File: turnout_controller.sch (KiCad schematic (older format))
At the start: 29 parts, among them J1 DCC_A, J2 DCC_B, J3 PROG, J4 MOT_CNTL, J5 MOT_POWER, J6 MOT_GND, J7 LED_1, J8 LED_2, SW1 SW_Push, SW2 SW_Push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

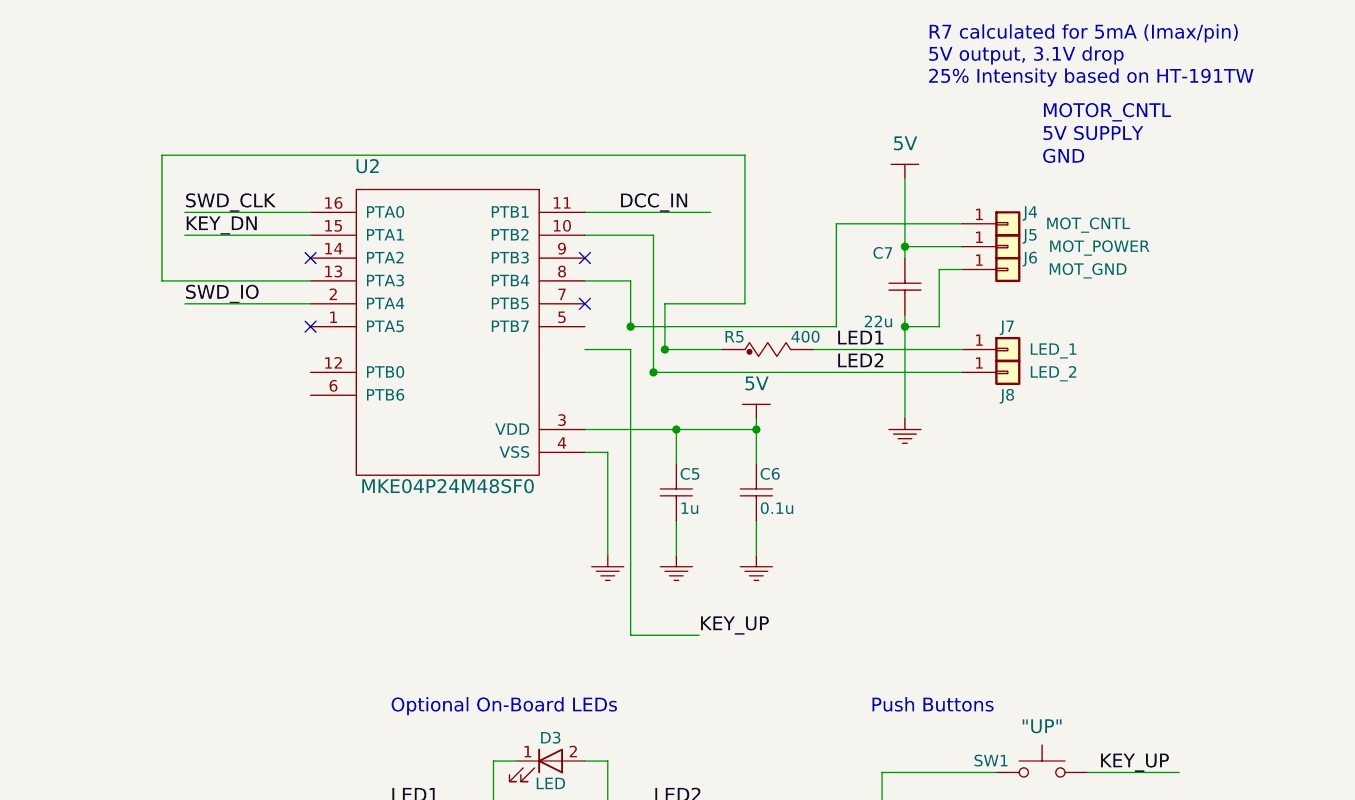
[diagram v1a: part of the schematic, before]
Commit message: Updated schematic for clarity. New Netlist. No PCB changes.
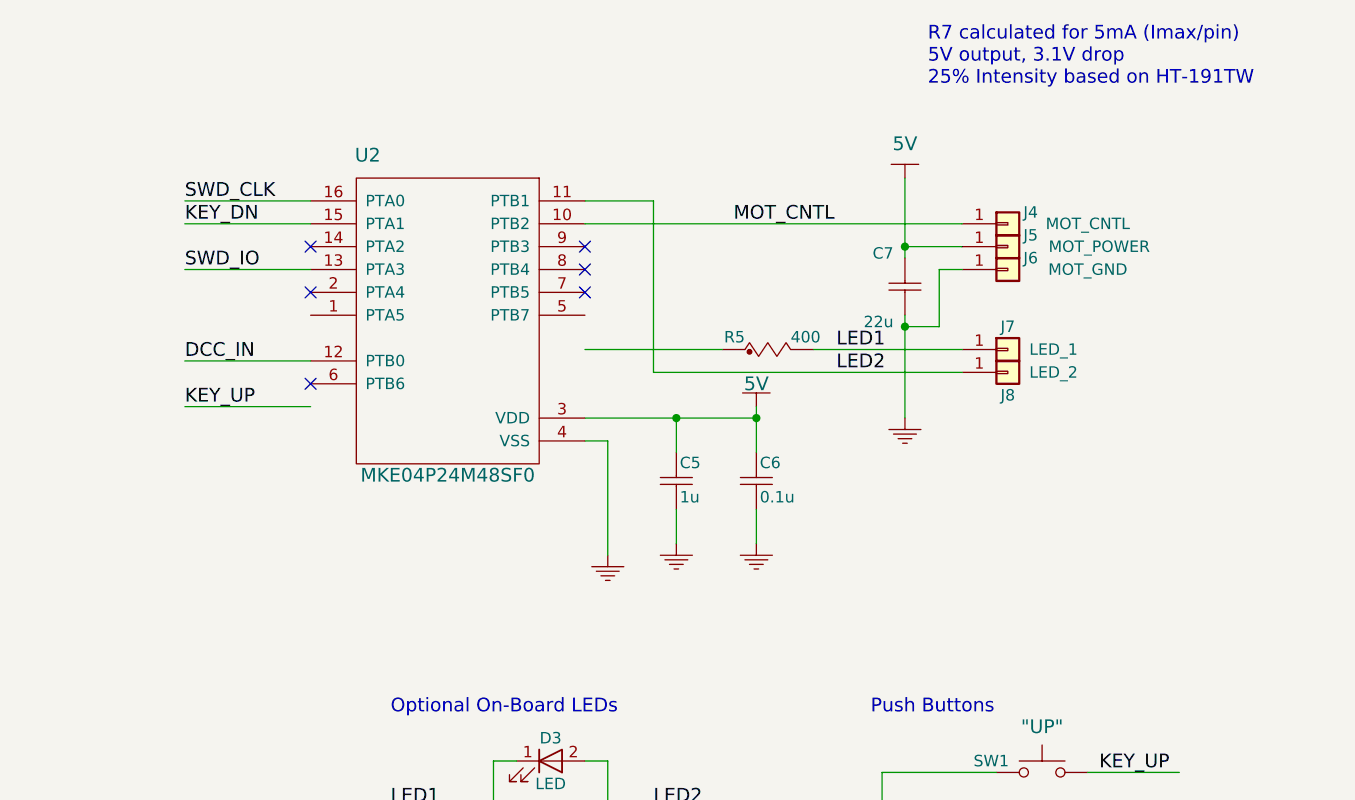
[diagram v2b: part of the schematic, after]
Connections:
- net labels added: MOT_CNTL
- wire segments 94 -> 82
- no-connect marks 4 -> 6
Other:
- note removed: "5V SUPPLY"
- note removed: "GND"
- note removed: "MOTOR_CNTL"
- moved on the sheet: C5, C6, U2
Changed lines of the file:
@@
 EESchema Schematic File Version 2
-LIBS:turnout_controller-rescue
 LIBS:power
 LIBS:device
@@
 L CAP_NP C5
 U 1 1 59FFDD6D
-P 8350 2750
-F 0 "C5" H 8365 2925 50  0000 L BNN
-F 1 "1u" H 8365 2775 50  0000 L BNN
-F 2 "Capacitors_SMD:C_0603_HandSoldering" H 8425 2650 40  0001 L BNN
-F 3 "" H 8350 2750 60  0000 C CNN
-F 4 "Volt" H 8450 2700 40  0001 L BNN "Voltage"
-	1    8350 2750
+P 8350 2700
+F 0 "C5" H 8365 2875 50  0000 L BNN
+F 1 "1u" H 8365 2725 50  0000 L BNN
+F 2 "Capacitors_SMD:C_0603_HandSoldering" H 8425 2600 40  0001 L BNN
+F 3 "" H 8350 2700 60  0000 C CNN
+F 4 "Volt" H 8450 2650 40  0001 L BNN "Voltage"
+	1    8350 2700
 	1    0    0    -1
 $EndComp
@@
 L CAP_NP C6
 U 1 1 59FFDDB1
-P 8700 2750
-F 0 "C6" H 8715 2925 50  0000 L BNN
-F 1 "0.1u" H 8715 2775 50  0000 L BNN
-F 2 "Capacitors_SMD:C_0603_HandSoldering" H 8775 2650 40  0001 L BNN
-F 3 "" H 8700 2750 60  0000 C CNN
-F 4 "Volt" H 8800 2700 40  0001 L BNN "Voltage"
-	1    8700 2750
-	1    0    0    -1
-$EndComp
-Text Notes 9950 1000 0    60   ~ 0
-MOTOR_CNTL
-Text Notes 9950 1100 0    60   ~ 0
-5V SUPPLY
-Text Notes 9950 1200 0    60   ~ 0
-GND
+P 8700 2700
+F 0 "C6" H 8715 2875 50  0000 L BNN
+F 1 "0.1u" H 8715 2725 50  0000 L BNN
+F 2 "Capacitors_SMD:C_0603_HandSoldering" H 8775 2600 40  0001 L BNN
+F 3 "" H 8700 2700 60  0000 C CNN
+F 4 "Volt" H 8800 2650 40  0001 L BNN "Voltage"
+	1    8700 2700
+	1    0    0    -1
+$EndComp
 $Comp
 L 12V #PWR01
@@
 L MKE04P24M48SF0-RESCUE-turnout_controller U2
 U 1 1 5A1255A7
-P 7350 2600
-F 0 "U2" H 7000 4000 60  0000 C CNN
-F 1 "MKE04P24M48SF0" H 7350 2600 60  0000 C CNN
-F 2 "Housings_SSOP:TSSOP-16_4.4x5mm_Pitch0.65mm" H 7350 2600 60  0001 C CNN
-F 3 "" H 7350 2600 60  0001 C CNN
-F 4 "MKE04P24M48SF0" H 7350 2600 60  0001 C CNN "MFG P/N"
-	1    7350 2600
+P 7350 2550
+F 0 "U2" H 7000 3950 60  0000 C CNN
+F 1 "MKE04P24M48SF0" H 7350 2550 60  0000 C CNN
+F 2 "Housings_SSOP:TSSOP-16_4.4x5mm_Pitch0.65mm" H 7350 2550 60  0001 C CNN
+F 3 "" H 7350 2550 60  0001 C CNN
+F 4 "MKE04P24M48SF0" H 7350 2550 60  0001 C CNN "MFG P/N"
+	1    7350 2550
 	1    0    0    -1
 $EndComp
@@
 L 5V #PWR03
 U 1 1 5A143044
-P 8700 2300
-F 0 "#PWR03" H 8700 2400 40  0001 C CNN
-F 1 "5V" H 8700 2450 60  0000 C CNN
-F 2 "" H 8700 2300 60  0000 C CNN
-F 3 "" H 8700 2300 60  0000 C CNN
-	1    8700 2300
+P 8700 2250
+F 0 "#PWR03" H 8700 2350 40  0001 C CNN
+F 1 "5V" H 8700 2350 60  0000 C CNN
+F 2 "" H 8700 2250 60  0000 C CNN
+F 3 "" H 8700 2250 60  0000 C CNN
+	1    8700 2250
 	1    0    0    -1
 $EndComp
@@
 L GND_ #PWR05
 U 1 1 5A143443
-P 8350 2950
-F 0 "#PWR05" H 8450 3050 30  0001 C CNN
-F 1 "GND_" H 8350 2850 30  0001 C CNN
-F 2 "" H 8350 2950 60  0000 C CNN
-F 3 "" H 8350 2950 60  0000 C CNN
-	1    8350 2950
+P 8350 2900
+F 0 "#PWR05" H 8450 3000 30  0001 C CNN
+F 1 "GND_" H 8350 2800 30  0001 C CNN
+F 2 "" H 8350 2900 60  0000 C CNN
+F 3 "" H 8350 2900 60  0000 C CNN
+	1    8350 2900
 	1    0    0    -1
 $EndComp
@@
 L GND_ #PWR06
 U 1 1 5A1434B7
-P 8700 2950
-F 0 "#PWR06" H 8800 3050 30  0001 C CNN
-F 1 "GND_" H 8700 2850 30  0001 C CNN
-F 2 "" H 8700 2950 60  0000 C CNN
-F 3 "" H 8700 2950 60  0000 C CNN
-	1    8700 2950
+P 8700 2900
+F 0 "#PWR06" H 8800 3000 30  0001 C CNN
+F 1 "GND_" H 8700 2800 30  0001 C CNN
+F 2 "" H 8700 2900 60  0000 C CNN
+F 3 "" H 8700 2900 60  0000 C CNN
+	1    8700 2900
 	1    0    0    -1
 $EndComp
@@
 	1    0    0    -1
 $EndComp
-Text Label 8100 1400 0    60   ~ 0
+Text Label 6200 2050 0    60   ~ 0
 DCC_IN
 $Comp
@@
 	1    0    0    -1
 $EndComp
-NoConn ~ 7950 1600
-NoConn ~ 7950 1800
-NoConn ~ 6750 1600
-Text Label 8450 3250 0    60   ~ 0
+NoConn ~ 6750 2150
+NoConn ~ 7950 1750
+NoConn ~ 6750 1550
+Text Label 6200 2250 0    60   ~ 0
 KEY_UP
-Text Label 6200 1500 0    60   ~ 0
+Text Label 6200 1450 0    60   ~ 0
 KEY_DN
 Text Label 10200 3850 0    60   ~ 0
@@
 	1    0    0    -1
 $EndComp
-Text Label 6200 1400 0    60   ~ 0
+Text Label 6200 1350 0    60   ~ 0
 SWD_CLK
-NoConn ~ 6750 1900
-Text Label 6200 1800 0    60   ~ 0
+NoConn ~ 6750 1750
+Text Label 6200 1650 0    60   ~ 0
 SWD_IO
 Text Label 7650 5400 0    60   ~ 0
@@
 $EndComp
 Wire Wire Line
-	7950 2450 8050 2450
-Wire Wire Line
-	7950 2350 8700 2350
-Connection ~ 8350 2350
-Wire Wire Line
-	8300 2000 8550 2000
-Wire Wire Line
-	8150 1900 9050 1900
+	7950 2400 8050 2400
 Wire Wire Line
 	8950 2000 9600 2000
@@
 	3850 2050 3850 2250
 Wire Wire Line
-	8350 2350 8350 2500
-Wire Wire Line
-	8700 2300 8700 2500
-Wire Wire Line
 	2200 3650 2200 3750
 Wire Wire Line
@@
 Wire Wire Line
 	2100 1250 2950 1250
-Wire Wire Line
-	7950 1400 8500 1400
 Wire Wire Line
 	1600 3150 1700 3150
@@
 Connection ~ 2200 3150
 Wire Wire Line
-	8050 2450 8050 2900
-Wire Wire Line
-	8350 2750 8350 2900
-Wire Wire Line
-	8700 2750 8700 2900
+	8050 2400 8050 2900
+Wire Wire Line
+	8350 2700 8350 2850
+Wire Wire Line
+	8700 2700 8700 2850
 Wire Wire Line
 	9350 1850 9350 2300
 Wire Wire Line
 	9500 1650 9600 1650
-Wire Wire Line
-	9050 1900 9050 1450
-Wire Wire Line
-	9050 1450 9600 1450
 Wire Wire Line
 	9350 1900 9500 1900
@@
 Connection ~ 9350 1900
 Wire Wire Line
-	6200 1500 6750 1500
+	6200 1450 6750 1450
 Wire Wire Line
 	3250 1650 3850 1650
-Connection ~ 8700 2350
 Wire Wire Line
 	10150 4100 10550 4100
@@
 	9600 1550 9350 1550
 Connection ~ 9350 1550
-Wire Wire Line
-	6750 1800 6200 1800
 Wire Wire Line
 	7450 5300 7950 5300
@@
 Connection ~ 8050 4000
 Wire Wire Line
-	8250 2100 9600 2100
-Wire Wire Line
 	7100 4000 7550 4000
 Wire Wire Line
@@
 	2250 5000 2200 5000
 Wire Wire Line
-	6750 1700 6100 1700
-Wire Wire Line
-	6100 1700 6100 1150
-Wire Wire Line
-	6100 1150 8650 1150
-Wire Wire Line
-	8650 1150 8650 1800
-Wire Wire Line
-	8650 1800 8300 1800
-Wire Wire Line
-	8300 1800 8300 2000
-Connection ~ 8300 2000
-Wire Wire Line
-	7950 1700 8150 1700
-Wire Wire Line
-	8150 1700 8150 1900
-Connection ~ 8150 1900
-Wire Wire Line
-	7950 1500 8250 1500
-Wire Wire Line
-	8250 1500 8250 2100
-Connection ~ 8250 2100
-Wire Wire Line
-	6200 1400 6750 1400
-Wire Wire Line
-	7950 2000 8150 2000
-Wire Wire Line
-	8150 2000 8150 3250
-Wire Wire Line
-	8150 3250 8450 3250
+	6200 1350 6750 1350
+Wire Wire Line
+	6750 2050 6200 2050
+Wire Wire Line
+	6750 2250 6200 2250
+Wire Wire Line
+	7950 1350 8250 1350
+Wire Wire Line
+	6750 1650 6200 1650
+Text Label 8600 1450 0    60   ~ 0
+MOT_CNTL
+Wire Wire Line
+	7950 1450 9600 1450
+NoConn ~ 7950 1550
+NoConn ~ 7950 1650
+Wire Wire Line
+	7950 2000 8550 2000
+Wire Wire Line
+	8250 1350 8250 2100
+Wire Wire Line
+	8250 2100 9600 2100
+Wire Wire Line
+	7950 2300 8700 2300
+Wire Wire Line
+	8350 2450 8350 2300
+Connection ~ 8350 2300
+Wire Wire Line
+	8700 2250 8700 2450
+Connection ~ 8700 2300
 $EndSCHEMATC

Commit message: Added component part numbers (including passives) and BOM.
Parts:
- C1, C4: MFG P/N (none) -> GRT188R61C106ME13D; Voltage Volt -> 16
- C2: MFG P/N (none) -> VJ0603V104ZXQPW1BC; Voltage Volt -> 10 VDC
- C3, C7: MFG P/N (none) -> GRT188R60J226ME13D; Voltage Volt -> 6.3
- C5: MFG P/N (none) -> 885012106010; Voltage Volt -> 10
- C6: MFG P/N (none) -> VJ0603V104ZXQPW1BC; Voltage Volt -> 10
- D1: MFG P/N SD1206S020S1R0 -> PMEG2010AEB,115
- D3, D4: MFG P/N (none) -> HT-191TW
- R1, R3: MFG P/N (none) -> CRCW060310K0JNEAC
- R2: MFG P/N (none) -> CRCW06034K70JNEAC‎
- R4: MFG P/N (none) -> ERA-3AED5492V
- R5: MFG P/N (none) -> PAT0603E4000BST1
- U1: MFG P/N (none) -> TPS561201DDCR
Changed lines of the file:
@@
 F 2 "Capacitors_SMD:C_0603_HandSoldering" H 3925 1700 40  0001 L BNN
 F 3 "" H 3850 1800 60  0000 C CNN
-F 4 "Volt" H 3950 1750 40  0001 L BNN "Voltage"
+F 4 "GRT188R61C106ME13D" H 3850 1800 60  0001 C CNN "MFG P/N"
+F 5 "16" H 3950 1750 40  0001 L BNN "Voltage"
 	1    3850 1800
 	-1   0    0    1
@@
 F 2 "Capacitors_SMD:C_0603_HandSoldering" H 8425 2600 40  0001 L BNN
 F 3 "" H 8350 2700 60  0000 C CNN
-F 4 "Volt" H 8450 2650 40  0001 L BNN "Voltage"
+F 4 "885012106010" H 8350 2700 60  0001 C CNN "MFG P/N"
+F 5 "10" H 8450 2650 40  0001 L BNN "Voltage"
 	1    8350 2700
 	1    0    0    -1
@@
 F 2 "Capacitors_SMD:C_0603_HandSoldering" H 8775 2600 40  0001 L BNN
 F 3 "" H 8700 2700 60  0000 C CNN
-F 4 "Volt" H 8800 2650 40  0001 L BNN "Voltage"
+F 4 "VJ0603V104ZXQPW1BC" H 8700 2700 60  0001 C CNN "MFG P/N"
+F 5 "10" H 8800 2650 40  0001 L BNN "Voltage"
 	1    8700 2700
 	1    0    0    -1
@@
 F 2 "Resistors_SMD:R_0603_HandSoldering" H 8650 2000 40  0001 L BNN
 F 3 "" H 8550 2050 60  0000 C CNN
-F 4 "Value" H 8550 2050 60  0001 C CNN "MFG"
-F 5 "Value" H 8550 2050 60  0001 C CNN "P/N"
+F 4 "PAT0603E4000BST1" H 8550 2050 60  0001 C CNN "MFG P/N"
+F 5 "Value" H 8550 2050 60  0001 C CNN "MFG"
+F 6 "Value" H 8550 2050 60  0001 C CNN "P/N"
 	1    8550 2050
 	1    0    0    -1
@@
 F 2 "Diodes_SMD:D_SOD-523" H 1450 3150 50  0001 C CNN
 F 3 "" H 1450 3150 50  0001 C CNN
-F 4 "SD1206S020S1R0" H 1450 3150 60  0001 C CNN "MFG P/N"
+F 4 "PMEG2010AEB,115" H 1450 3150 60  0001 C CNN "MFG P/N"
 	1    1450 3150
 	-1   0    0    1
@@
 F 2 "Resistors_SMD:R_0603_HandSoldering" H 2250 3200 40  0001 L BNN
 F 3 "" H 2150 3250 60  0000 C CNN
+F 4 "CRCW06034K70JNEAC‎" V 2150 3250 60  0001 C CNN "MFG P/N"
 	1    2150 3250
 	0    1    1    0
@@
 F 2 "Resistors_SMD:R_0603_HandSoldering" H 1800 3150 40  0001 L BNN
 F 3 "" H 1700 3200 60  0000 C CNN
+F 4 "CRCW060310K0JNEAC" H 1700 3200 60  0001 C CNN "MFG P/N"
 	1    1700 3200
 	1    0    0    -1
@@
 F 2 "Capacitors_SMD:C_0603_HandSoldering" H 9425 1500 40  0001 L BNN
 F 3 "" H 9350 1600 60  0000 C CNN
-F 4 "Volt" H 9450 1550 40  0001 L BNN "Voltage"
+F 4 "GRT188R60J226ME13D" H 9350 1600 60  0001 C CNN "MFG P/N"
+F 5 "6.3" H 9450 1550 40  0001 L BNN "Voltage"
 	1    9350 1600
 	-1   0    0    1
@@
 F 2 "LEDs:LED_0603" H 7800 4200 50  0001 C CNN
 F 3 "" H 7800 4200 50  0001 C CNN
+F 4 "HT-191TW" H 7800 4200 60  0001 C CNN "MFG P/N"
 	1    7800 4200
 	-1   0    0    1
@@
 F 2 "LEDs:LED_0603" H 7800 3800 50  0001 C CNN
 F 3 "" H 7800 3800 50  0001 C CNN
+F 4 "HT-191TW" H 7800 3800 60  0001 C CNN "MFG P/N"
 	1    7800 3800
 	1    0    0    -1
@@
 F 2 "TO_SOT_Packages_SMD:SOT-23-6_Handsoldering" H 1700 5400 60  0001 C CNN
 F 3 "" H 1700 5400 60  0001 C CNN
+F 4 "TPS561201DDCR" H 1700 5400 60  0001 C CNN "MFG P/N"
 	1    1700 5400
 	1    0    0    -1
@@
 F 2 "Resistors_SMD:R_0603_HandSoldering" H 2600 5250 40  0001 L BNN
 F 3 "" H 2500 5300 60  0000 C CNN
+F 4 "CRCW060310K0JNEAC" H 2500 5300 60  0001 C CNN "MFG P/N"
 	1    2500 5300
 	0    1    1    0
@@
 F 2 "Resistors_SMD:R_0603_HandSoldering" H 2750 5200 40  0001 L BNN
 F 3 "" H 2650 5250 60  0000 C CNN
+F 4 "ERA-3AED5492V" H 2650 5250 60  0001 C CNN "MFG P/N"
 	1    2650 5250
 	1    0    0    -1
@@
 F 2 "Capacitors_SMD:C_0603_HandSoldering" H 1175 5450 40  0001 L BNN
 F 3 "" H 1100 5550 60  0000 C CNN
-F 4 "Volt" H 1200 5500 40  0001 L BNN "Voltage"
+F 4 "GRT188R61C106ME13D" H 1100 5550 60  0001 C CNN "MFG P/N"
+F 5 "16" H 1200 5500 40  0001 L BNN "Voltage"
 	1    1100 5550
 	1    0    0    -1
@@
 F 2 "Capacitors_SMD:C_0603_HandSoldering" H 3225 5500 40  0001 L BNN
 F 3 "" H 3150 5600 60  0000 C CNN
-F 4 "Volt" H 3250 5550 40  0001 L BNN "Voltage"
+F 4 "GRT188R60J226ME13D" H 3150 5600 60  0001 C CNN "MFG P/N"
+F 5 "6.3" H 3250 5550 40  0001 L BNN "Voltage"
 	1    3150 5600
 	1    0    0    -1
@@
 F 2 "Capacitors_SMD:C_0603_HandSoldering" H 2325 4900 40  0001 L BNN
 F 3 "" H 2250 5000 60  0000 C CNN
-F 4 "Volt" H 2350 4950 40  0001 L BNN "Voltage"
+F 4 "10 VDC" H 2350 4950 40  0001 L BNN "Voltage"
+F 5 "VJ0603V104ZXQPW1BC" V 2250 5000 60  0001 C CNN "MFG P/N"
 	1    2250 5000
 	0    1    1    0
